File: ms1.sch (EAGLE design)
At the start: 123 parts, among them IC1 MAX3232EUE, J1 POWERPOLE_POWER25A, J10 RS485, J11 I2C, J12 TTL_SERIAL, J13 Radio, J14 RS232, J2 RAIN, J3 ADC1, J4 ON, J5 D1, J6 D2, J7 ADC2, J8 LED-EN, Q1 DMG6602SVT, Q2 DMG6602SVT, Q3 DMG6602SVT, Q4 DMG6602SVT, U1 LT1934ES6TRMPBF, U2 LT1934ES6TRMPBF, U3 DS3231SN, U4 ISL3179EIBZ, X1 KUSBVX-BS1N

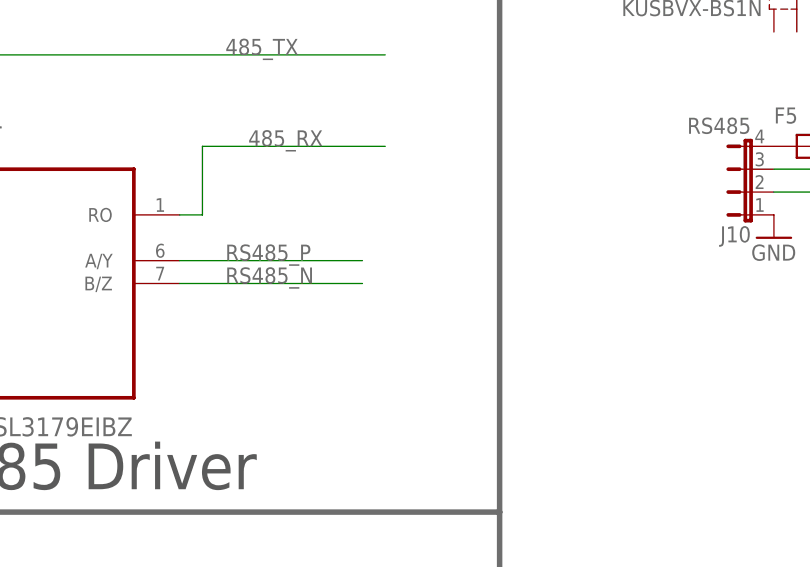
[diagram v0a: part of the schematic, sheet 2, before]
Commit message: fixes #2 now has rs483 termination resistor
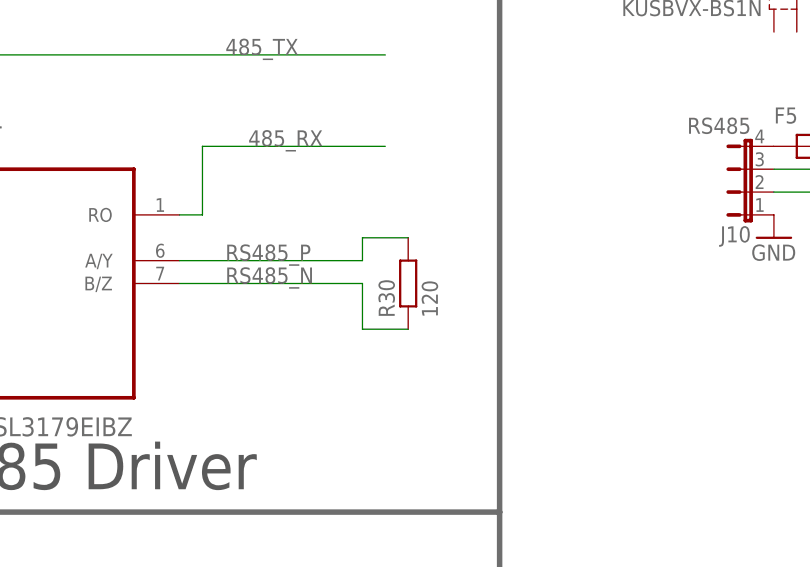
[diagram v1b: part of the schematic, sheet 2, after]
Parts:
- added R30: 120, resistor:R-EU_R0805
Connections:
- net RS485_N: now also R30.1
- net RS485_P: now also R30.2
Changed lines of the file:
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@@
 <part name="F7" library="farnell-parts" deviceset="MCF0805" device=""/>
 <part name="F8" library="farnell-parts" deviceset="MCF0805" device=""/>
+<part name="R30" library="resistor" deviceset="R-EU_" device="R0805" value="120"/>
 </parts>
 <sheets>
@@
 <instance part="F5" gate="G$1" x="276.86" y="86.36"/>
 <instance part="F6" gate="G$1" x="322.58" y="88.9"/>
+<instance part="R30" gate="G$1" x="231.14" y="71.12" rot="R90"/>
 </instances>
 <busses>
@@
 <label x="210.82" y="71.12" size="1.778" layer="95"/>
 <pinref part="U4" gate="A" pin="B/Z"/>
+<pinref part="R30" gate="G$1" pin="1"/>
+<wire x1="231.14" y1="66.04" x2="226.06" y2="66.04" width="0.1524" layer="91"/>
+<wire x1="226.06" y1="66.04" x2="226.06" y2="71.12" width="0.1524" layer="91"/>
 </segment>
 <segment>
@@
 <wire x1="205.74" y1="73.66" x2="226.06" y2="73.66" width="0.1524" layer="91"/>
 <label x="210.82" y="73.66" size="1.778" layer="95"/>
-</segment>
-<segment>
+<wire x1="226.06" y1="73.66" x2="226.06" y2="76.2" width="0.1524" layer="91"/>
+<pinref part="R30" gate="G$1" pin="2"/>
+<wire x1="226.06" y1="76.2" x2="231.14" y2="76.2" width="0.1524" layer="91"/>
+</segment>
+<segment>

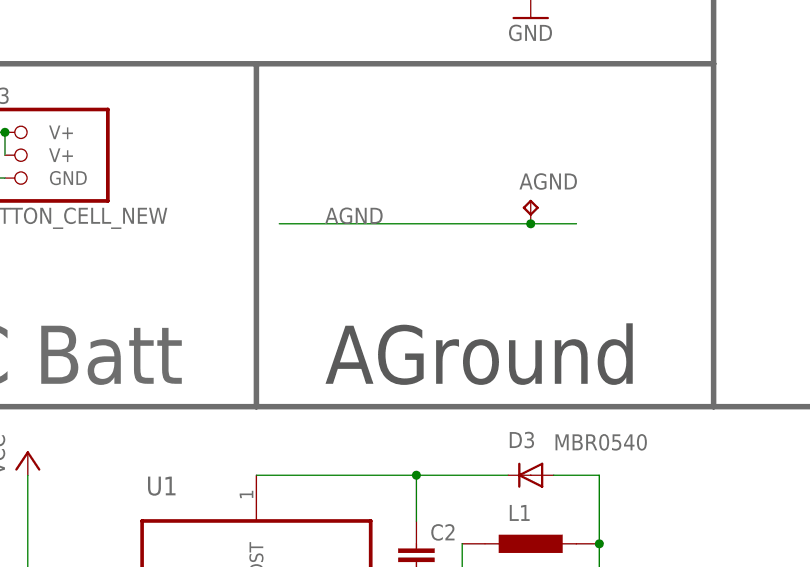
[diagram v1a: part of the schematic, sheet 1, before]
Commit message: fixes #7 now has gnd link header
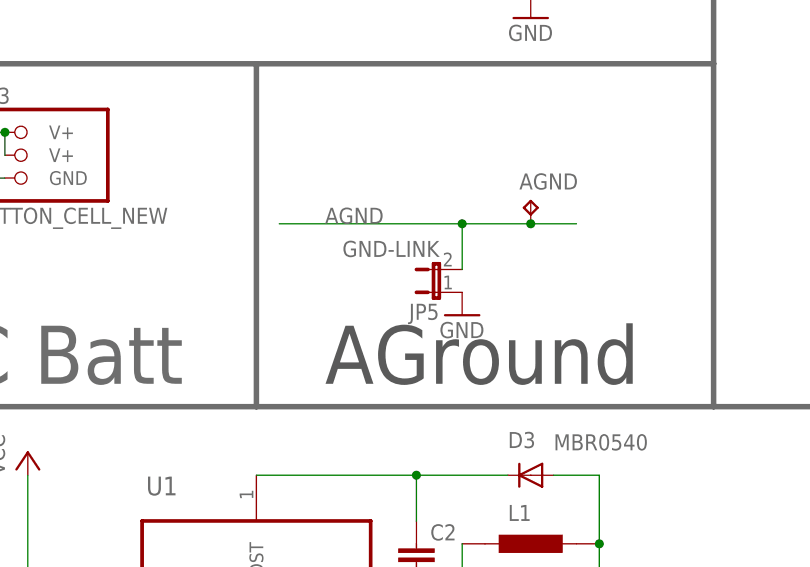
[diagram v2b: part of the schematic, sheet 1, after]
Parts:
- added JP5: GND-LINK, jumper:JP1E
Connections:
- net AGND: now also JP5.2
- net GND: now also JP5.1
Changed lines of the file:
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@@
 <part name="F8" library="farnell-parts" deviceset="MCF0805" device=""/>
 <part name="R30" library="resistor" deviceset="R-EU_" device="R0805" value="120"/>
+<part name="GND1" library="supply1" deviceset="GND" device=""/>
+<part name="JP5" library="jumper" deviceset="JP1E" device="" value="GND-LINK"/>
 </parts>
 <sheets>
@@
 <instance part="F7" gate="G$1" x="63.5" y="43.18"/>
 <instance part="F8" gate="G$1" x="63.5" y="66.04"/>
+<instance part="GND1" gate="1" x="76.2" y="193.04"/>
+<instance part="JP5" gate="A" x="73.66" y="195.58" rot="R90"/>
 </instances>
 <busses>
@@
 <pinref part="R1" gate="G$1" pin="1"/>
 <pinref part="GND16" gate="1" pin="GND"/>
+</segment>
+<segment>
+<pinref part="GND1" gate="1" pin="GND"/>
+<pinref part="JP5" gate="A" pin="1"/>
 </segment>
 </net>
@@
 </segment>
 <segment>
-<wire x1="55.88" y1="203.2" x2="83.82" y2="203.2" width="0.1524" layer="91"/>
+<wire x1="55.88" y1="203.2" x2="76.2" y2="203.2" width="0.1524" layer="91"/>
 <pinref part="AGND" gate="G$1" pin="TP"/>
+<wire x1="76.2" y1="203.2" x2="83.82" y2="203.2" width="0.1524" layer="91"/>
 <wire x1="83.82" y1="203.2" x2="88.9" y2="203.2" width="0.1524" layer="91"/>
 <junction x="83.82" y="203.2"/>
 <label x="60.96" y="203.2" size="1.778" layer="95"/>
-</segment>
-<segment>
+<wire x1="76.2" y1="198.12" x2="76.2" y2="203.2" width="0.1524" layer="91"/>
+<junction x="76.2" y="203.2"/>
+<pinref part="JP5" gate="A" pin="2"/>
+</segment>
+<segment>

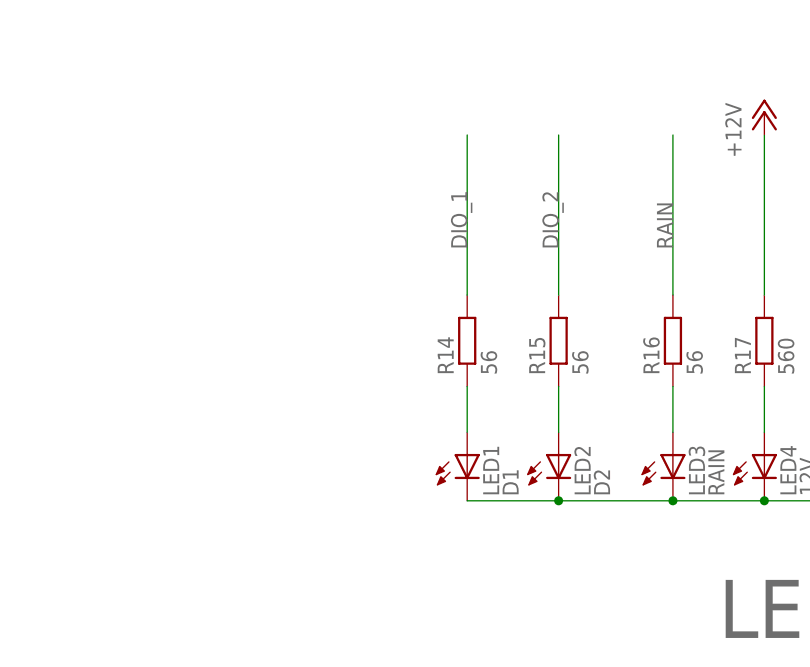
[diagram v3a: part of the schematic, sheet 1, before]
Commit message: DIO remapped to be TXEN for rs485, new DIO pin not yet selected
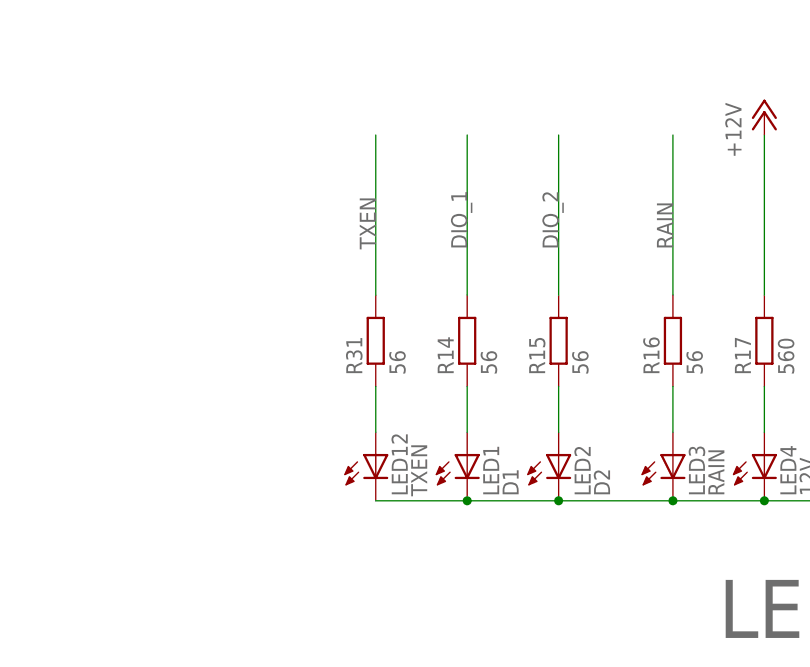
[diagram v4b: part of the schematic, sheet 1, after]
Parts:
- removed R27: 1K, resistor:R-EU_R0805
- added LED12: TXEN, led:LEDCHIP-LED0805
- added R31: 56, resistor:R-EU_R0805
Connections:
- removed net N$10: R27.1, U4.DE
- new net N$27: LED12.A, R31.1
- new net TXEN: R31.2, U$5.CA0, U4.DE, U4.~RE
- net 485_3V3: no longer R27.2
- net DIO_2: no longer U$5.CA0
- net GND: no longer U4.~RE
- net LGND: now also LED12.C
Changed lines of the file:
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@@
 <part name="C20" library="glacsweb" deviceset="C-EU" device="C0805" value="100nF"/>
 <part name="GND10" library="glacsweb" deviceset="GND" device=""/>
-<part name="R27" library="resistor" deviceset="R-EU_" device="R0805" value="1K"/>
 <part name="JP3" library="SparkFun-Passives" deviceset="JUMPER-2" device="SMD-NC"/>
 <part name="J13" library="farnell-parts" deviceset="5-PIN-MOLEX" device="" value="Radio"/>
@@
 <part name="GND1" library="supply1" deviceset="GND" device=""/>
 <part name="JP5" library="jumper" deviceset="JP1E" device="" value="GND-LINK"/>
+<part name="LED12" library="led" deviceset="LED" device="CHIP-LED0805" value="TXEN"/>
+<part name="R31" library="resistor" deviceset="R-EU_" device="R0805" value="56"/>
 </parts>
 <sheets>
@@
 <instance part="GND1" gate="1" x="76.2" y="193.04"/>
 <instance part="JP5" gate="A" x="73.66" y="195.58" rot="R90"/>
+<instance part="LED12" gate="G$1" x="243.84" y="208.28"/>
+<instance part="R31" gate="G$1" x="243.84" y="220.98" rot="R90"/>
 </instances>
 <busses>
@@
 <junction x="287.02" y="203.2"/>
 <pinref part="LED1" gate="G$1" pin="C"/>
+<wire x1="243.84" y1="203.2" x2="254" y2="203.2" width="0.1524" layer="91"/>
+<pinref part="LED12" gate="G$1" pin="C"/>
+<junction x="254" y="203.2"/>
 </segment>
 </net>
@@
 <pinref part="J5" gate="G$1" pin="1"/>
 <pinref part="F8" gate="G$1" pin="P$2"/>
+</segment>
+</net>
+<net name="N$27" class="0">
+<segment>
+<pinref part="LED12" gate="G$1" pin="A"/>
+<pinref part="R31" gate="G$1" pin="1"/>
+<wire x1="243.84" y1="215.9" x2="243.84" y2="210.82" width="0.1524" layer="91"/>
+</segment>
+</net>
+<net name="TXEN" class="0">
+<segment>
+<wire x1="243.84" y1="226.06" x2="243.84" y2="243.84" width="0.1524" layer="91"/>
+<label x="243.84" y="231.14" size="1.778" layer="95" rot="R90"/>
+<pinref part="R31" gate="G$1" pin="2"/>
 </segment>
 </net>
@@
 </instance>
 <instance part="GND10" gate="1" x="165.1" y="58.42"/>
-<instance part="R27" gate="G$1" x="157.48" y="73.66" rot="R90"/>
 <instance part="IC1" gate="G$1" x="187.96" y="154.94"/>
 <instance part="IC1" gate="P" x="187.96" y="129.54" rot="R90"/>
@@
 <pinref part="GND10" gate="1" pin="GND"/>
 <pinref part="U4" gate="A" pin="GND"/>
-<pinref part="U4" gate="A" pin="~RE"/>
-<wire x1="170.18" y1="73.66" x2="165.1" y2="73.66" width="0.1524" layer="91"/>
-<wire x1="165.1" y1="73.66" x2="165.1" y2="63.5" width="0.1524" layer="91"/>
 <junction x="165.1" y="63.5"/>
 <pinref part="C20" gate="G$1" pin="2"/>
@@
 </segment>
 </net>
-<net name="N$10" class="0">
-<segment>
-<pinref part="U4" gate="A" pin="DE"/>
-<wire x1="170.18" y1="71.12" x2="162.56" y2="71.12" width="0.1524" layer="91"/>
-<wire x1="162.56" y1="71.12" x2="162.56" y2="68.58" width="0.1524" layer="91"/>
-<pinref part="R27" gate="G$1" pin="1"/>
-<wire x1="162.56" y1="68.58" x2="157.48" y2="68.58" width="0.1524" layer="91"/>
-</segment>
-</net>
 <net name="N$59" class="0">
 <segment>
@@
 <net name="485_3V3" class="0">
 <segment>
-<wire x1="170.18" y1="78.74" x2="157.48" y2="78.74" width="0.1524" layer="91"/>
-<wire x1="157.48" y1="78.74" x2="152.4" y2="78.74" width="0.1524" layer="91"/>
+<wire x1="170.18" y1="78.74" x2="152.4" y2="78.74" width="0.1524" layer="91"/>
 <wire x1="152.4" y1="75.184" x2="152.4" y2="78.74" width="0.1524" layer="91"/>
 <pinref part="U4" gate="A" pin="VCC"/>
 <pinref part="C20" gate="G$1" pin="1"/>
-<pinref part="R27" gate="G$1" pin="2"/>
-<junction x="157.48" y="78.74"/>
 <label x="152.4" y="78.74" size="1.778" layer="95"/>
 </segment>
@@
 <pinref part="J14" gate="G$1" pin="4"/>
 <pinref part="F6" gate="G$1" pin="P$1"/>
-</segment>
-</net>
-<net name="DIO_2" class="0">
-<segment>
-<pinref part="U$5" gate="G$1" pin="CA0"/>
-<wire x1="38.1" y1="177.8" x2="20.32" y2="177.8" width="0.1524" layer="91"/>
-<label x="20.32" y="177.8" size="1.778" layer="95"/>
 </segment>
 </net>
@@
 </segment>
 </net>
+<net name="TXEN" class="0">
+<segment>
+<pinref part="U4" gate="A" pin="~RE"/>
+<wire x1="170.18" y1="73.66" x2="154.94" y2="73.66" width="0.1524" layer="91"/>
+<pinref part="U4" gate="A" pin="DE"/>
+<wire x1="170.18" y1="71.12" x2="170.18" y2="73.66" width="0.1524" layer="91"/>
+<junction x="170.18" y="73.66"/>
+<label x="154.94" y="73.66" size="1.778" layer="95"/>
+</segment>
+<segment>
+<pinref part="U$5" gate="G$1" pin="CA0"/>
+<wire x1="38.1" y1="177.8" x2="20.32" y2="177.8" width="0.1524" layer="91"/>
+<label x="20.32" y="177.8" size="1.778" layer="95"/>
+</segment>
+</net>

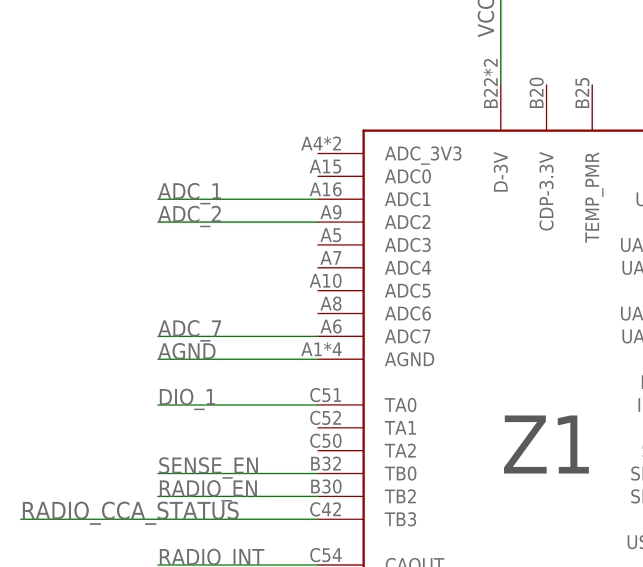
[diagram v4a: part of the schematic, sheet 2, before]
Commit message: Fixes #1 DIO_2 now on ADC5 which can be used for digital IO, and the hack permenantly routed to rs485 driver
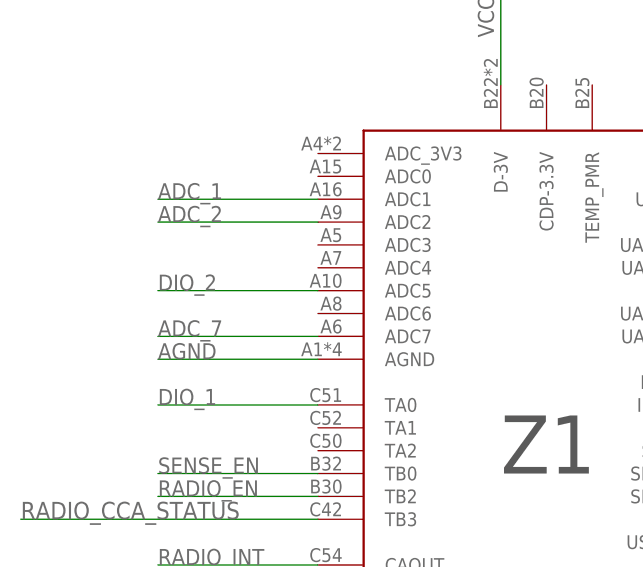
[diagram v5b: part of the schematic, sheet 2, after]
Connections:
- net DIO_2: now also U$5.ADC5
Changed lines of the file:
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@@
 <?xml version="1.0" encoding="utf-8"?>
 <!DOCTYPE eagle SYSTEM "eagle.dtd">
-<eagle version="6.5.0">
+<eagle version="6.6.0">
 <drawing>
 <settings>
@@
 </segment>
 </net>
+<net name="DIO_2" class="0">
+<segment>
+<pinref part="U$5" gate="G$1" pin="ADC5"/>
+<wire x1="38.1" y1="210.82" x2="20.32" y2="210.82" width="0.1524" layer="91"/>
+<label x="20.32" y="210.82" size="1.778" layer="95"/>
+</segment>
+</net>

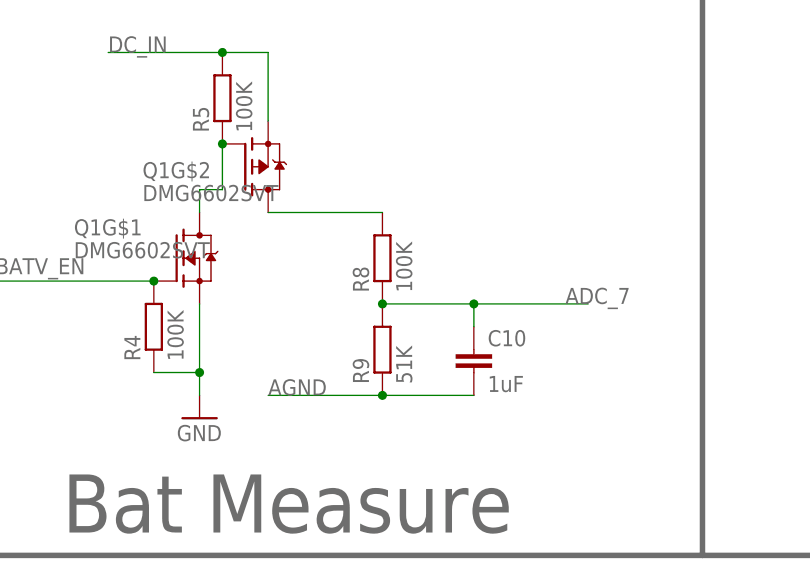
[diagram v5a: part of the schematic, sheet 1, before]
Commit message: now with correct values for batv divider
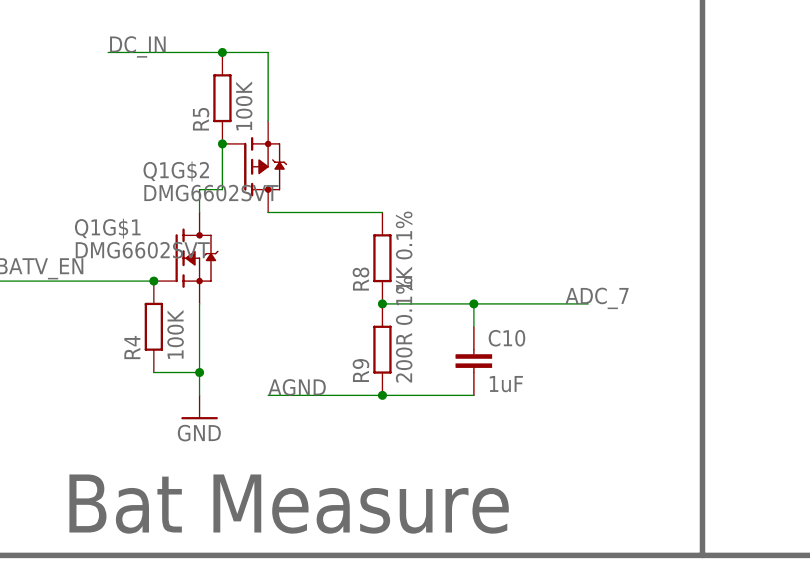
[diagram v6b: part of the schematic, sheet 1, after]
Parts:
- R8: value 100K -> 1K 0.1%
- R9: value 51K -> 200R 0.1%
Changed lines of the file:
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@@
 <?xml version="1.0" encoding="utf-8"?>
 <!DOCTYPE eagle SYSTEM "eagle.dtd">
-<eagle version="6.6.0">
+<eagle version="6.5.0">
 <drawing>
 <settings>
@@
 <part name="J12" library="farnell-parts" deviceset="4-PIN-MOLEX" device="" value="TTL_SERIAL"/>
 <part name="GND9" library="supply1" deviceset="GND" device=""/>
-<part name="R9" library="resistor" deviceset="R-EU_" device="R0805" value="51K"/>
-<part name="R8" library="resistor" deviceset="R-EU_" device="R0805" value="100K"/>
+<part name="R9" library="resistor" deviceset="R-EU_" device="R0805" value="200R 0.1%"/>
+<part name="R8" library="resistor" deviceset="R-EU_" device="R0805" value="1K 0.1%"/>
 <part name="C10" library="resistor" deviceset="C-EU" device="C0805" value="1uF"/>
 <part name="GND11" library="supply1" deviceset="GND" device=""/>
